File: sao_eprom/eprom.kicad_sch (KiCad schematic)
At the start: 15 parts, among them U1 27C512, U2 74HC273, U3 74HC273, U4 PCAL6416APW

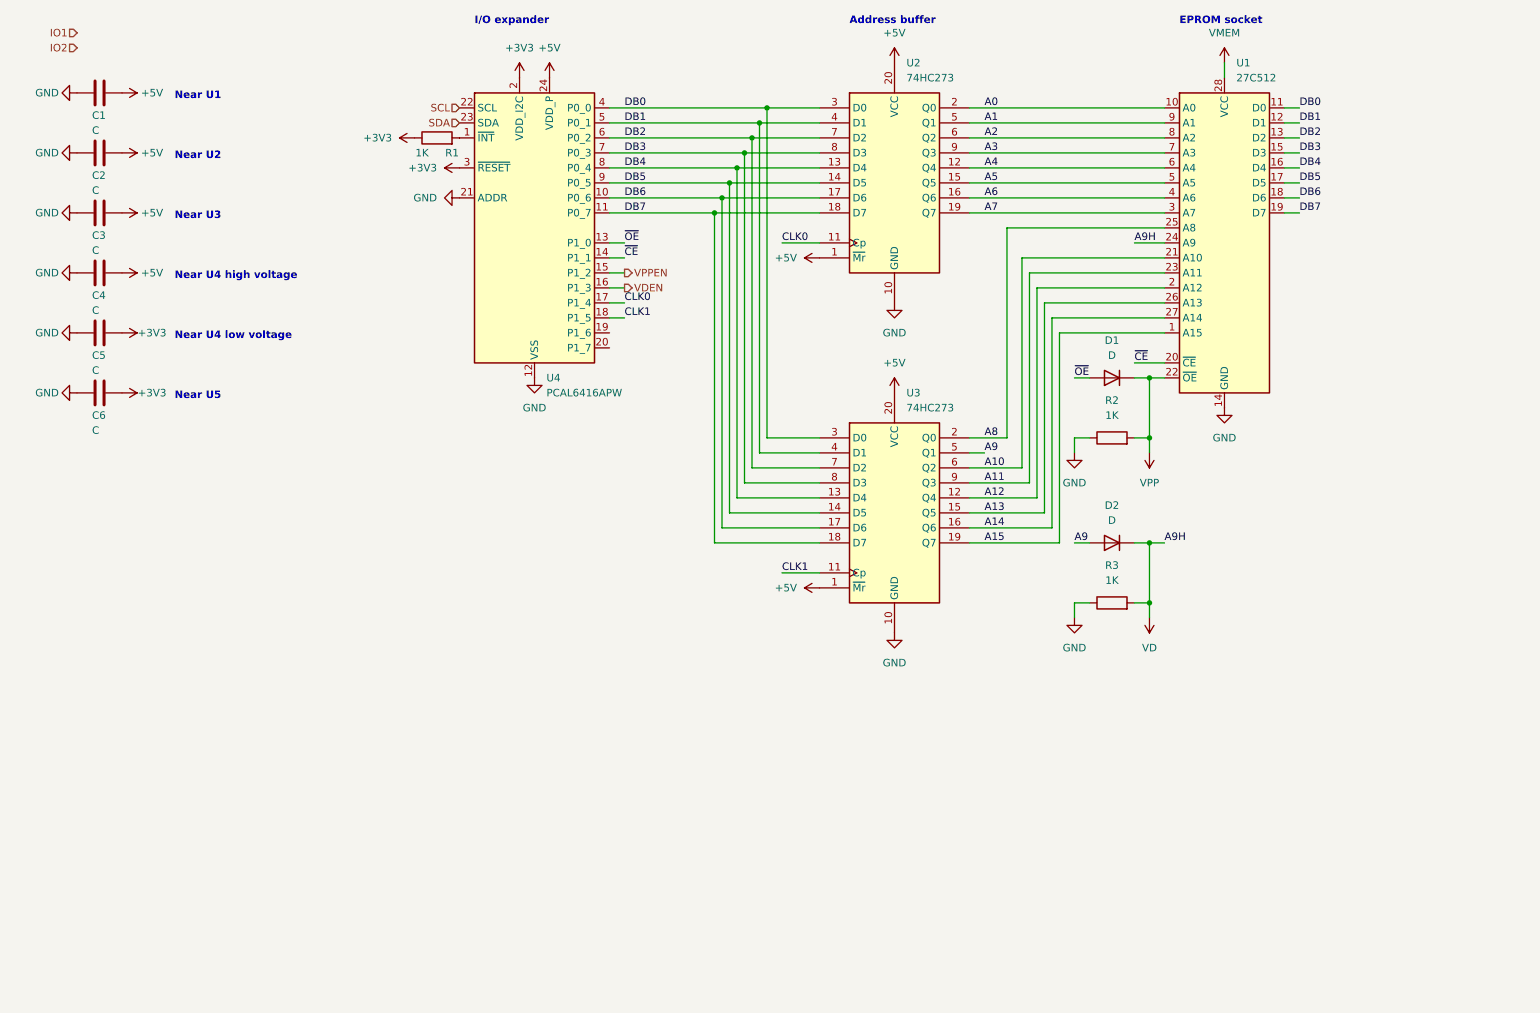
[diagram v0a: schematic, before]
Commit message: Reworks the address circuit
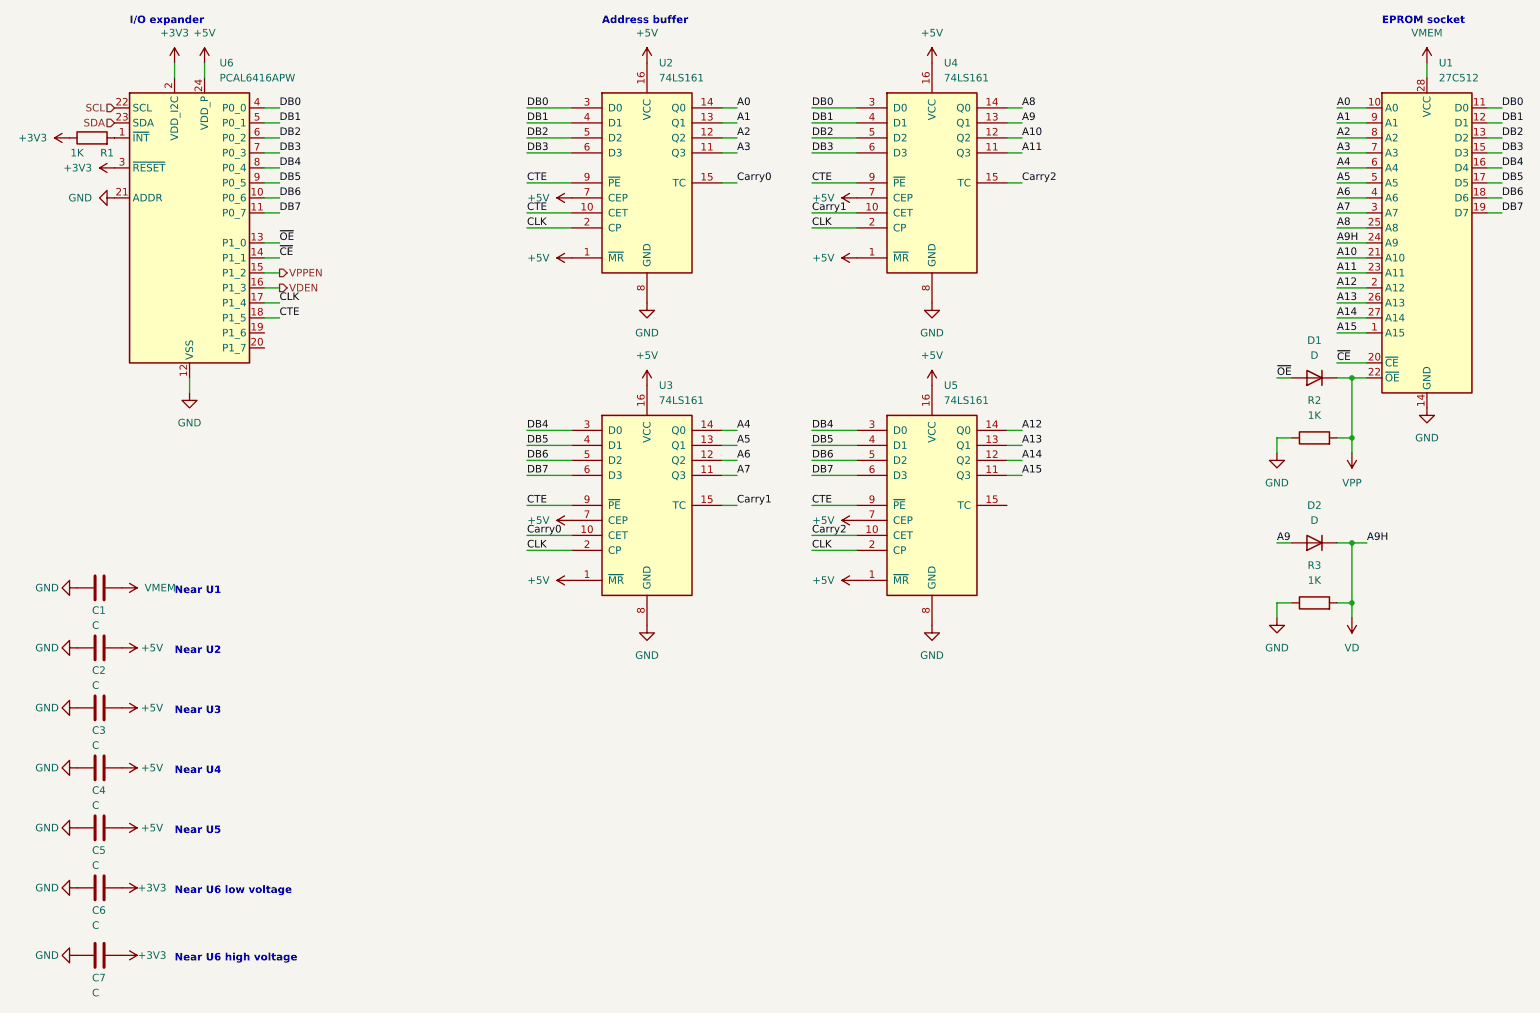
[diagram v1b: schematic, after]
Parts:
- removed U2, U3: 74HC273, symbol 74xx:74HC273
- added C7: C, Capacitor_THT:C_Disc_D3.0mm_W1.6mm_P2.50mm, symbol Device:C
- added U2, U3, U4, U5: 74LS161, Package_DIP:DIP-16_W7.62mm, symbol 74xx:74LS161
- D1, D2: footprint (none) -> Diode_THT:D_DO-41_SOD81_P10.16mm_Horizontal
- R1, R2, R3: footprint (none) -> Resistor_THT:R_Axial_DIN0207_L6.3mm_D2.5mm_P7.62mm_Horizontal
- renumbered U4 to U6
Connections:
- net +3V3: now also C7.1; no longer C5.1
- net +5V: now also C5.1, U2.1 (~{MR}), U2.16 (VCC), U2.7 (CEP), U3.1 (~{MR}), U3.16 (VCC), U3.7 (CEP), U4.1 (~{MR}), U4.16 (VCC), U4.7 (CEP), U5.1 (~{MR}), U5.16 (VCC), U5.7 (CEP); no longer C1.1
- net A0: now also U2.14 (Q0)
- net A1: now also U2.13 (Q1)
- net A10: now also U4.12 (Q2)
- net A11: now also U4.11 (Q3)
- net A12: now also U5.14 (Q0)
- net A13: now also U5.13 (Q1)
- net A14: now also U5.12 (Q2)
- net A15: now also U5.11 (Q3)
- net A2: now also U2.12 (Q2)
- net A3: now also U2.11 (Q3)
- net A4: now also U3.14 (Q0)
- net A5: now also U3.13 (Q1)
- net A6: now also U3.12 (Q2)
- net A7: now also U3.11 (Q3)
- net A8: now also U4.14 (Q0)
- net A9: now also U4.13 (Q1)
- net DB0: now also U2.3 (D0), U4.3 (D0)
- net DB1: now also U2.4 (D1), U4.4 (D1)
- net DB2: now also U2.5 (D2), U4.5 (D2)
- net DB3: now also U2.6 (D3), U4.6 (D3)
- net DB4: now also U3.3 (D0), U5.3 (D0)
- net DB5: now also U3.4 (D1), U5.4 (D1)
- net DB6: now also U3.5 (D2), U5.5 (D2)
- net DB7: now also U3.6 (D3), U5.6 (D3)
- net GND: now also C7.2, U2.8 (GND), U3.8 (GND), U4.8 (GND), U5.8 (GND)
- net VMEM: now also C1.1
- net CLK0 renamed CLK
- net CLK: now also U2.2 (CP), U3.2 (CP), U4.2 (CP), U5.2 (CP)
- net CLK1 renamed CTE
- net CTE: now also U2.10 (CET), U2.9 (~{PE}), U3.9 (~{PE}), U4.9 (~{PE}), U5.9 (~{PE})
- new net Carry0: U2.15 (TC), U3.10 (CET)
- new net Carry1: U3.15 (TC), U4.10 (CET)
- new net Carry2: U4.15 (TC), U5.10 (CET)
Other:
- note added: "Near U4"
- note added: "Near U6 high voltage"
- note added: "Near U6 low voltage"
- note removed: "Near U4 high voltage"
- note removed: "Near U4 low voltage"
- moved on the sheet: C1, C2, C3, C4, C5, C6, D1, D2, R1, R2, R3, U1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

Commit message: Finish the first design revision
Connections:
- net +3V3: no longer C7.1
- net +5V: now also C7.1
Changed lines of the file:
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@@
+    (pin "1")
+  )
+  (symbol (lib_id "power:+5V") (at 34.29 179.07 270) (unit 1)
+    (in_bom yes) (on_board yes) (fields_autoplaced)
+    (property "Reference" "#PWR0102" (id 0) (at 30.48 179.07 0)
+      (effects (font (size 1.27 1.27)) hide)
+    )
+    (property "Value" "+5V" (id 1) (at 38.1 179.0699 90)
+      (effects (font (size 1.27 1.27)) (justify left))
+    )
+    (property "Footprint" "" (id 2) (at 34.29 179.07 0)
+      (effects (font (size 1.27 1.27)) hide)
+    )
+    (property "Datasheet" "" (id 3) (at 34.29 179.07 0)
+      (effects (font (size 1.27 1.27)) hide)
+    )
     (pin "1")
   )
@@
       (effects (font (size 1.27 1.27)) hide)
     )
-    (pin "1")
-  )
-  (symbol (lib_name "+3V3_2") (lib_id "power:+3V3") (at 34.29 179.07 270) (unit 1)
-    (in_bom yes) (on_board yes)
-    (property "Reference" "#PWR023" (id 0) (at 30.48 179.07 0)
-      (effects (font (size 1.27 1.27)) hide)
-    )
-    (property "Value" "+3V3" (id 1) (at 39.37 179.07 90))
-    (property "Footprint" "" (id 2) (at 34.29 179.07 0)
-      (effects (font (size 1.27 1.27)) hide)
-    )
-    (property "Datasheet" "" (id 3) (at 34.29 179.07 0)
-      (effects (font (size 1.27 1.27)) hide)
-    )

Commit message: Do some resistor calculations
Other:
- title: (none) -> EPROM interface
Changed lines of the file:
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@@
 (kicad_sch (version 20211123) (generator eeschema)
   (paper "A4")
+  (title_block
+    (title "EPROM interface")
+  )
   (junction (at 242.57 91.44) (diameter 0) (color 0 0 0 0)
   )

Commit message: Prepare for the ORDERING
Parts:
- D1, D2: value D -> RL207
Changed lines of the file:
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@@
     (in_bom yes) (on_board yes) (fields_autoplaced)
     (property "Reference" "D1" (id 0) (at 236.22 74.93 0))
-    (property "Value" "D" (id 1) (at 236.22 77.47 0))
+    (property "Value" "RL207" (id 1) (at 236.22 77.47 0))
     (property "Footprint" "Diode_THT:D_DO-41_SOD81_P10.16mm_Horizontal" (id 2) (at 236.22 81.28 0)
       (effects (font (size 1.27 1.27)) hide)
@@
     (in_bom yes) (on_board yes) (fields_autoplaced)
     (property "Reference" "D2" (id 0) (at 236.22 102.87 0))
-    (property "Value" "D" (id 1) (at 236.22 105.41 0))
+    (property "Value" "RL207" (id 1) (at 236.22 105.41 0))
     (property "Footprint" "Diode_THT:D_DO-41_SOD81_P10.16mm_Horizontal" (id 2) (at 236.22 109.22 0)
       (effects (font (size 1.27 1.27)) hide)
